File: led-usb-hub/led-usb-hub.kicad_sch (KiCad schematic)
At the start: 132 parts, among them J1 USBC_USB2.0, J2 RGBUSB_54-00266, J3 RGBUSB_54-00266, J4 RGBUSB_54-00266, J5 SWD, SW1 RESET, SW2 BOOLSEL, SW3 LED_EN, U1 RP2040, U10 ESDS312D, U11 ESDS312D, U12 TC54VN3002, U13 W25Q16JVSN, U2 TPS2042D, U3 TPS2042D, U4 TPS563257DRLR, U5 TPS563257DRLR, U6 TUSB2046IBVF, U7 ESDS312D, U8 ESDS312D, U9 ESDS312D, Y1 12Mhz, Y2 6Mhz

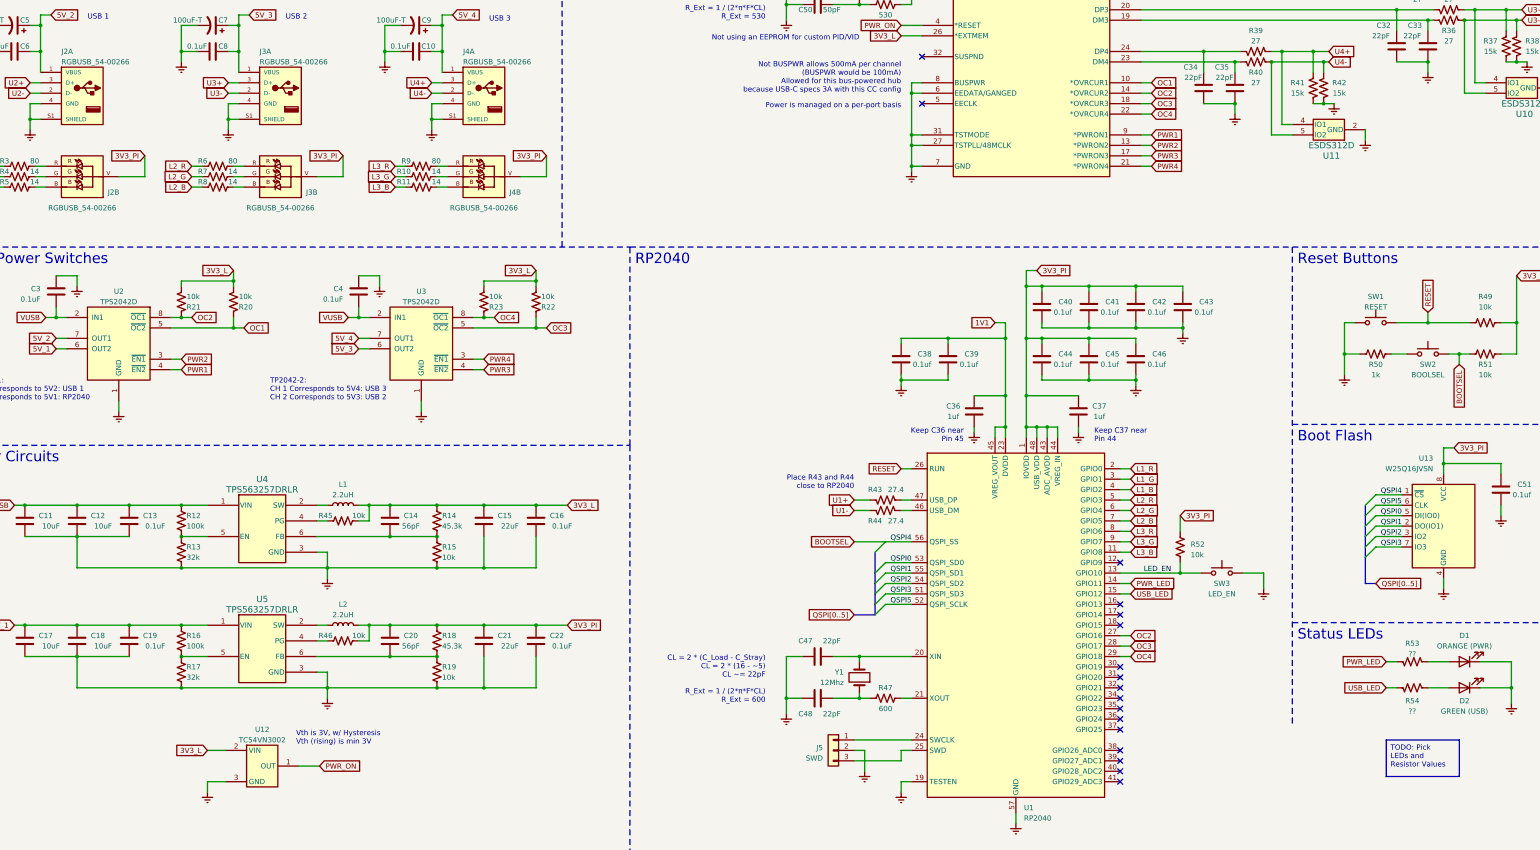
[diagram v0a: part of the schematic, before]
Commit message: Spec LEDs TODO: Footprints and models for KSS221 Switches TODO: spec inductors and tantalum caps Then layout (but also find all the rest of the passives necessary, some sizes may change)
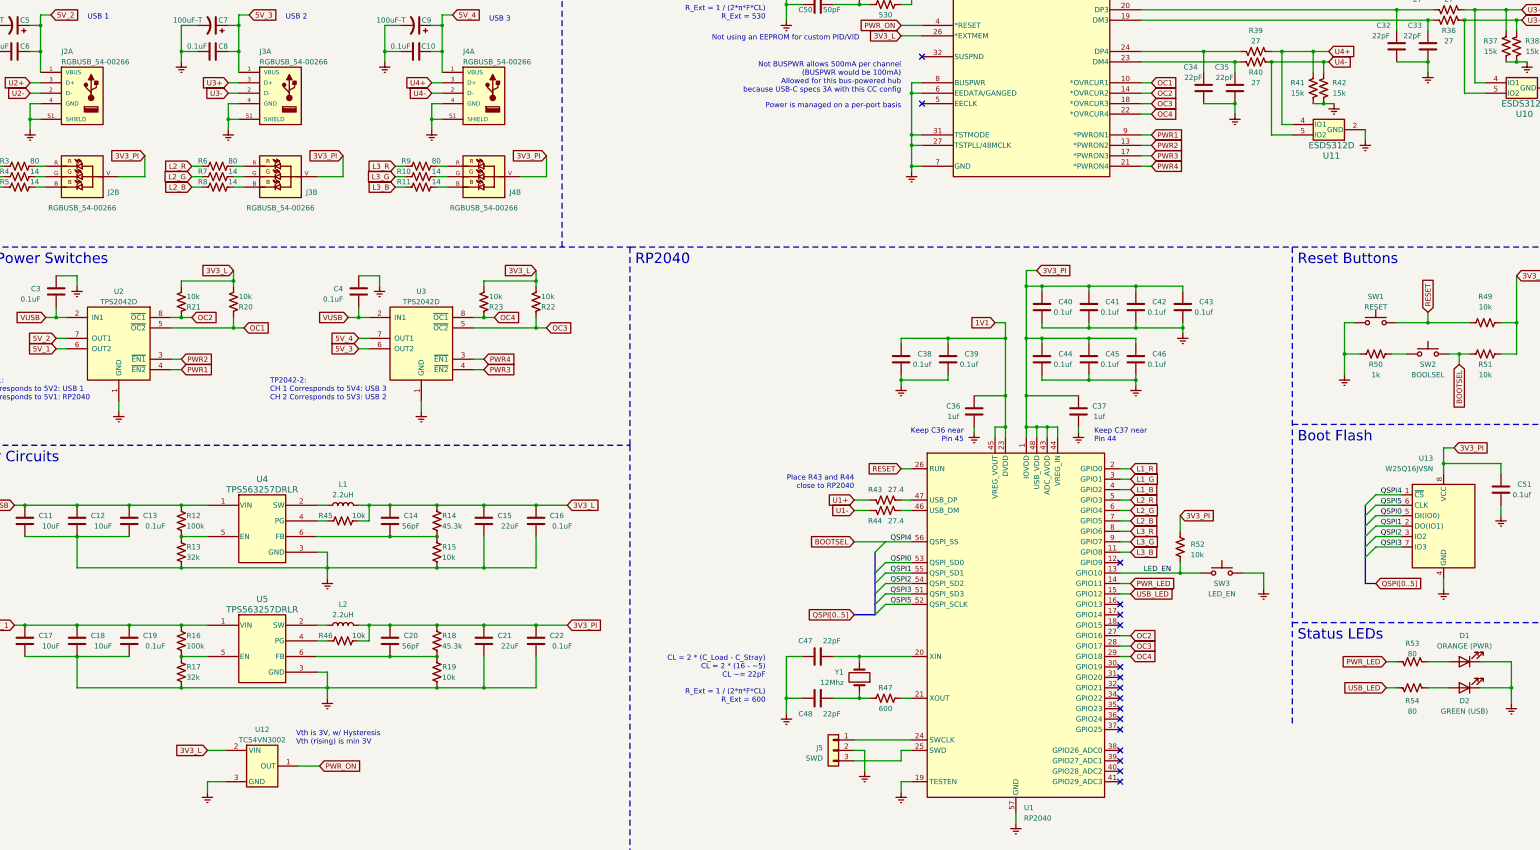
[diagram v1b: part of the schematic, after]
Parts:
- D1, D2: footprint (none) -> LED_SMD:LED_0603_1608Metric_Pad1.05x0.95mm_HandSolder
- R53, R54: value ?? -> 80
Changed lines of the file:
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@@
     (stroke (width 0) (type default))
   )
-  (text_box "TODO: Pick LEDs and Resistor Values"
-    (at 360.68 256.54 0) (size 17.78 8.89)
-    (stroke (width 0) (type default))
-    (fill (type color) (color 0 255 255 0.24))
-    (effects (font (size 1.27 1.27)) (justify left top))
-  )
   (text "USB 2\n" (at 92.71 81.28 0)
     (effects (font (size 1.27 1.27)) (justify left bottom))
@@
       (effects (font (size 1.27 1.27)))
     )
-    (property "Footprint" "" (at 379.73 237.49 0)
+    (property "Footprint" "LED_SMD:LED_0603_1608Metric_Pad1.05x0.95mm_HandSolder" (at 379.73 237.49 0)
       (effects (font (size 1.27 1.27)) hide)
     )
@@
       (effects (font (size 1.27 1.27)))
     )
-    (property "Value" "??" (at 367.03 235.585 90)
+    (property "Value" "80" (at 367.03 235.585 90)
       (effects (font (size 1.27 1.27)))
     )
@@
       (effects (font (size 1.27 1.27)))
     )
-    (property "Value" "??" (at 367.03 249.555 90)
+    (property "Value" "80" (at 367.03 249.555 90)
       (effects (font (size 1.27 1.27)))
     )
@@
       (effects (font (size 1.27 1.27)))
     )
-    (property "Footprint" "" (at 379.73 243.84 0)
+    (property "Footprint" "LED_SMD:LED_0603_1608Metric_Pad1.05x0.95mm_HandSolder" (at 379.73 243.84 0)
       (effects (font (size 1.27 1.27)) hide)
     )

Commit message: Add Footprints and models for switches TODO: Spec all passives to finalize footprints (if staying at 0603) TODO: Find Inductor and C-T footprints Then it's layout
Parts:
- SW1, SW2, SW3: footprint (none) -> KSS221GLFS:SW_KSS221GLFS
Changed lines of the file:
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@@
       (effects (font (size 1.27 1.27)))
     )
-    (property "Footprint" "" (at 320.675 210.82 0)
+    (property "Footprint" "KSS221GLFS:SW_KSS221GLFS" (at 320.675 210.82 0)
       (effects (font (size 1.27 1.27)) hide)
     )
@@
       (effects (font (size 1.27 1.27)))
     )
-    (property "Footprint" "" (at 370.84 157.48 0)
+    (property "Footprint" "KSS221GLFS:SW_KSS221GLFS" (at 370.84 157.48 0)
       (effects (font (size 1.27 1.27)) hide)
     )
@@
       (effects (font (size 1.27 1.27)))
     )
-    (property "Footprint" "" (at 358.14 149.86 0)
+    (property "Footprint" "KSS221GLFS:SW_KSS221GLFS" (at 358.14 149.86 0)
       (effects (font (size 1.27 1.27)) hide)
     )

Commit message: Unify values a bit
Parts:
- C36, C37: value 1uf -> 1uF
- C38, C39, C40, C41, C42, C43, C44, C45, C46, C51: value 0.1uf -> 0.1uF
- R43, R44: value 27.4 -> 27
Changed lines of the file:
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@@
       (effects (font (size 1.27 1.27)))
     )
-    (property "Value" "0.1uf" (at 393.7 196.85 0)
+    (property "Value" "0.1uF" (at 393.7 196.85 0)
       (effects (font (size 1.27 1.27)))
     )
@@
       (effects (font (size 1.27 1.27)))
     )
-    (property "Value" "27.4" (at 241.3 195.58 90)
+    (property "Value" "27" (at 241.3 195.58 90)
       (effects (font (size 1.27 1.27)))
     )
@@
       (effects (font (size 1.27 1.27)))
     )
-    (property "Value" "0.1uf" (at 281.94 152.4 0)
+    (property "Value" "0.1uF" (at 281.94 152.4 0)
       (effects (font (size 1.27 1.27)))
     )
@@
       (effects (font (size 1.27 1.27)))
     )
-    (property "Value" "0.1uf" (at 259.08 165.1 0)
+    (property "Value" "0.1uF" (at 259.08 165.1 0)
       (effects (font (size 1.27 1.27)))
     )
@@
       (effects (font (size 1.27 1.27)))
     )
-    (property "Value" "0.1uf" (at 281.94 165.1 0)
+    (property "Value" "0.1uF" (at 281.94 165.1 0)
       (effects (font (size 1.27 1.27)))
     )
@@
       (effects (font (size 1.27 1.27)))
     )
-    (property "Value" "0.1uf" (at 316.23 152.4 0)
+    (property "Value" "0.1uF" (at 316.23 152.4 0)
       (effects (font (size 1.27 1.27)))
     )
@@
       (effects (font (size 1.27 1.27)))
     )
-    (property "Value" "0.1uf" (at 293.37 165.1 0)
+    (property "Value" "0.1uF" (at 293.37 165.1 0)
       (effects (font (size 1.27 1.27)))
     )
@@
       (effects (font (size 1.27 1.27)))
     )
-    (property "Value" "1uf" (at 290.83 177.8 0)
+    (property "Value" "1uF" (at 290.83 177.8 0)
       (effects (font (size 1.27 1.27)))
     )
@@
       (effects (font (size 1.27 1.27)))
     )
-    (property "Value" "0.1uf" (at 247.65 165.1 0)
+    (property "Value" "0.1uF" (at 247.65 165.1 0)
       (effects (font (size 1.27 1.27)))
     )
@@
       (effects (font (size 1.27 1.27)))
     )
-    (property "Value" "27.4" (at 241.3 203.2 90)
+    (property "Value" "27" (at 241.3 203.2 90)
       (effects (font (size 1.27 1.27)))
     )
@@
       (effects (font (size 1.27 1.27)))
     )
-    (property "Value" "0.1uf" (at 304.8 165.1 0)
+    (property "Value" "0.1uF" (at 304.8 165.1 0)
       (effects (font (size 1.27 1.27)))
     )
@@
       (effects (font (size 1.27 1.27)))
     )
-    (property "Value" "1uf" (at 255.27 177.8 0)
+    (property "Value" "1uF" (at 255.27 177.8 0)
       (effects (font (size 1.27 1.27)))
     )
@@
       (effects (font (size 1.27 1.27)))
     )
-    (property "Value" "0.1uf" (at 304.8 152.4 0)
+    (property "Value" "0.1uF" (at 304.8 152.4 0)
       (effects (font (size 1.27 1.27)))
     )
@@
       (effects (font (size 1.27 1.27)))
     )
-    (property "Value" "0.1uf" (at 293.37 152.4 0)
+    (property "Value" "0.1uF" (at 293.37 152.4 0)
       (effects (font (size 1.27 1.27)))
     )

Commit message: All Components have first pass footprints, need to go through all passives to verify
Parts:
- C5, C7, C9: footprint (none) -> Capacitor_Tantalum_SMD:CP_EIA-3528-15_AVX-H_Pad1.50x2.35mm_HandSolder
- L1, L2: footprint (none) -> Inductor_SMD:L_1210_3225Metric_Pad1.42x2.65mm_HandSolder
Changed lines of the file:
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@@
       (effects (font (size 1.27 1.27)) (justify right))
     )
-    (property "Footprint" "" (at 74.93 82.55 0)
+    (property "Footprint" "Capacitor_Tantalum_SMD:CP_EIA-3528-15_AVX-H_Pad1.50x2.35mm_HandSolder" (at 74.93 82.55 0)
       (effects (font (size 1.27 1.27)) hide)
     )
@@
       (effects (font (size 1.27 1.27)))
     )
-    (property "Footprint" "" (at 106.68 199.39 0)
+    (property "Footprint" "Inductor_SMD:L_1210_3225Metric_Pad1.42x2.65mm_HandSolder" (at 106.68 199.39 0)
       (effects (font (size 1.27 1.27)) hide)
     )
@@
       (effects (font (size 1.27 1.27)) (justify right))
     )
-    (property "Footprint" "" (at 124.46 82.55 0)
+    (property "Footprint" "Capacitor_Tantalum_SMD:CP_EIA-3528-15_AVX-H_Pad1.50x2.35mm_HandSolder" (at 124.46 82.55 0)
       (effects (font (size 1.27 1.27)) hide)
     )
@@
       (effects (font (size 1.27 1.27)))
     )
-    (property "Footprint" "" (at 106.68 228.6 0)
+    (property "Footprint" "Inductor_SMD:L_1210_3225Metric_Pad1.42x2.65mm_HandSolder" (at 106.68 228.6 0)
       (effects (font (size 1.27 1.27)) hide)
     )
@@
       (effects (font (size 1.27 1.27)) (justify right))
     )
-    (property "Footprint" "" (at 26.67 82.55 0)
+    (property "Footprint" "Capacitor_Tantalum_SMD:CP_EIA-3528-15_AVX-H_Pad1.50x2.35mm_HandSolder" (at 26.67 82.55 0)
       (effects (font (size 1.27 1.27)) hide)
     )

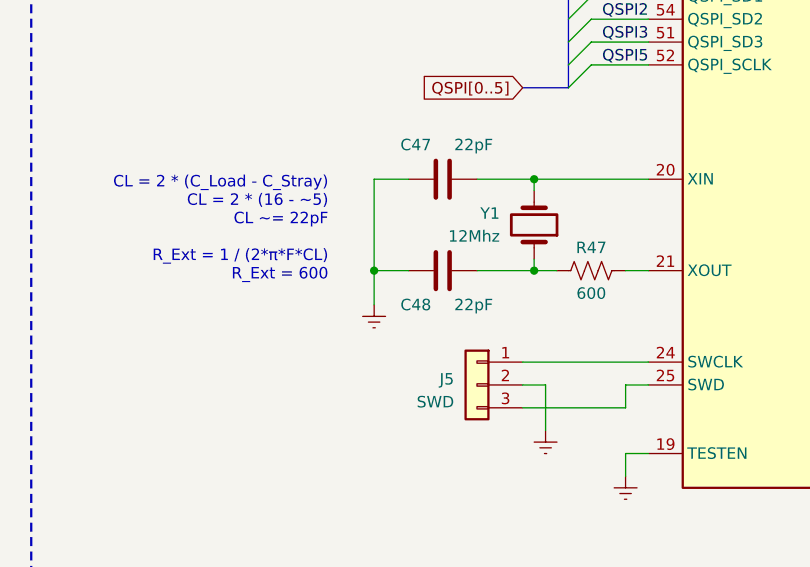
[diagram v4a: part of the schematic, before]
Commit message: Fit Crystal Series Resistor value better
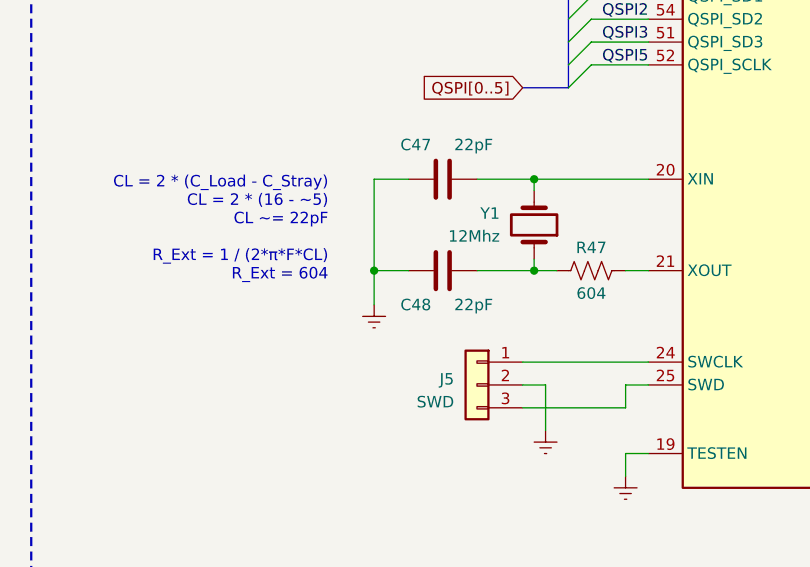
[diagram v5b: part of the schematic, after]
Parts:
- R47: value 600 -> 604
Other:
- note added: "CL = 2 * (C_Load - C_Stray) CL = 2 * (16 - ~5) CL ~= 22pF R_Ext = 1 / (2*π*F*CL) R_Ext = 604"
- note removed: "CL = 2 * (C_Load - C_Stray) CL = 2 * (16 - ~5) CL ~= 22pF R_Ext = 1 / (2*π*F*CL) R_Ext = 600"
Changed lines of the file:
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@@
     (effects (font (size 1.27 1.27)) (justify left bottom))
   )
-  (text "CL = 2 * (C_Load - C_Stray)\nCL = 2 * (16 - ~5)\nCL ~= 22pF\n\nR_Ext = 1 / (2*π*F*CL)\nR_Ext = 600 "
+  (text "CL = 2 * (C_Load - C_Stray)\nCL = 2 * (16 - ~5)\nCL ~= 22pF\n\nR_Ext = 1 / (2*π*F*CL)\nR_Ext = 604"
     (at 209.55 247.65 0)
     (effects (font (size 1.27 1.27)) (justify right bottom))
@@
       (effects (font (size 1.27 1.27)))
     )
-    (property "Value" "600" (at 238.76 248.92 90)
+    (property "Value" "604" (at 238.76 248.92 90)
       (effects (font (size 1.27 1.27)))
     )

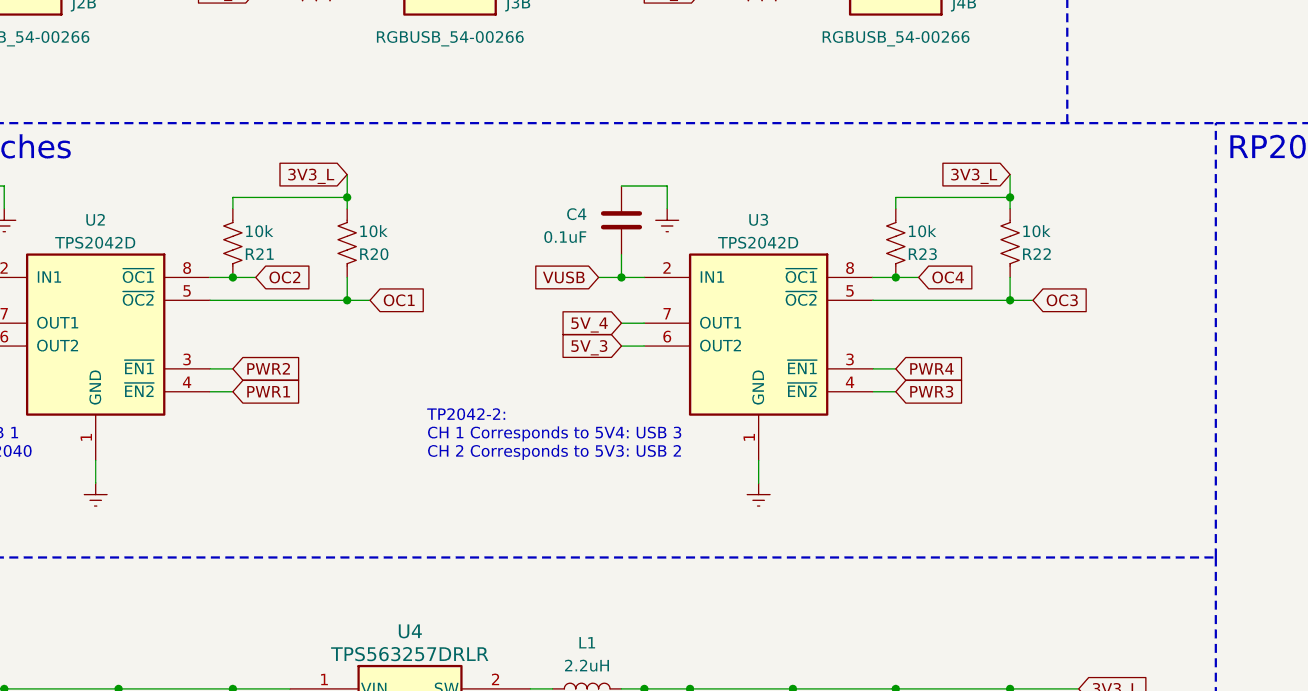
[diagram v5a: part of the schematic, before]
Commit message: Add 0.1uF decoupling caps for USB Power Switches, rec by TI
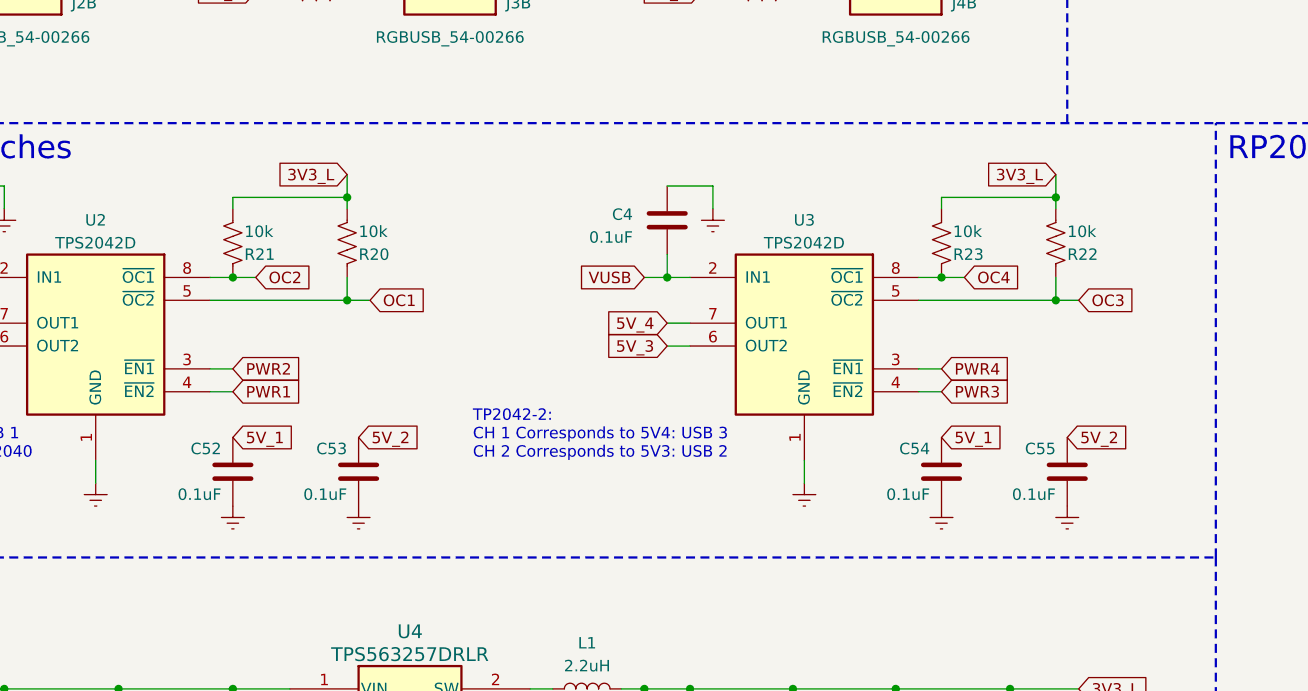
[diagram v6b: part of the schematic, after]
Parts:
- added C52, C53, C54, C55: 0.1uF, Capacitor_SMD:C_0603_1608Metric_Pad1.08x0.95mm_HandSolder, symbol Device:C
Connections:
- net 5V_1: now also C52.1, C54.1
- net 5V_2: now also C53.1, C55.1
- net Earth: now also C52.2, C53.2, C54.2, C55.2
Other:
- moved on the sheet: C4, R22, R23, U3

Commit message: Switch TVS diode for one that's easier to route Figure out how to route diff traces
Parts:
- removed U10, U11, U7, U8, U9: ESDS312D, Package_TO_SOT_SMD:SOT-23-5, symbol ESDS312:ESDS312DBVR
- added U10, U11, U7, U8, U9: TPD2EUSB30, DRT0003A, symbol TPD2EUSB30DRTR:TPD2EUSB30
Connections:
- net Earth: now also U10.3 (GND), U11.3 (GND), U7.3 (GND), U8.3 (GND), U9.3 (GND); no longer J1.S1 (SHIELD)
- net U1+: now also U8.1 (IO1)
- net U1-: now also U8.2 (IO2)
- net U2+: now also U9.1 (IO1)
- net U2-: now also U9.2 (IO2)
- net U3+: now also U10.1 (IO1)
- net U3-: now also U10.2 (IO2)
- net U4+: now also U11.1 (IO1)
- net U4-: now also U11.2 (IO2)
- net UD'+: now reaches C26.1, R24.2, R25.1, U6.1 (DP0)
- net UD'+: now also U7.1 (IO1); no longer C27.1, R26.1, U6.2 (DM0)
- net U3'+: now reaches C32.1, R35.1, U6.20 (DP3)
- net U1'+: now reaches C28.1, R27.1, U6.12 (DP1)
- net U3'-: now reaches C33.1, R36.1, U6.19 (DM3)
- net U1'-: now reaches C29.1, R28.1, U6.11 (DM1)
- net U4'+: now reaches C34.1, R39.1, U6.24 (DP4)
- net U2'-: now reaches C31.1, R32.1, U6.15 (DM2)
- net U2'+: now reaches C30.1, R31.1, U6.16 (DP2)
- net U4'-: now reaches C35.1, R40.1, U6.23 (DM4)
- new net UD'-: C27.1, R26.1, U6.2 (DM0), U7.2 (IO2)
- no-connect marks 19 -> 20
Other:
- moved on the sheet: C1, C2, J1, R1, R2
